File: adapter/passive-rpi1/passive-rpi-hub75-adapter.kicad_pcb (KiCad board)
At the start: 2 copper layers, 37 x 19 mm, 2 parts, among them P1 RPi-Header

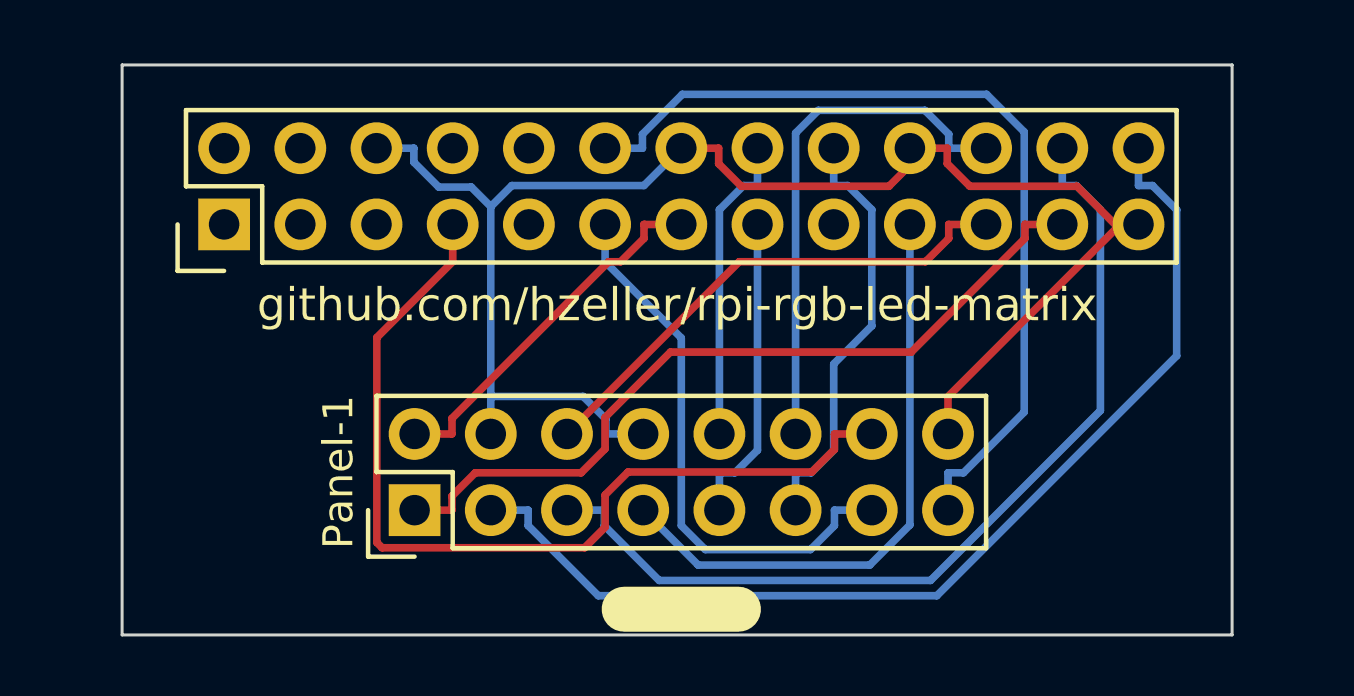
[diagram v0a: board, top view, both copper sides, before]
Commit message: o the connector is ambiguous, so make labelling a bit more obvious.
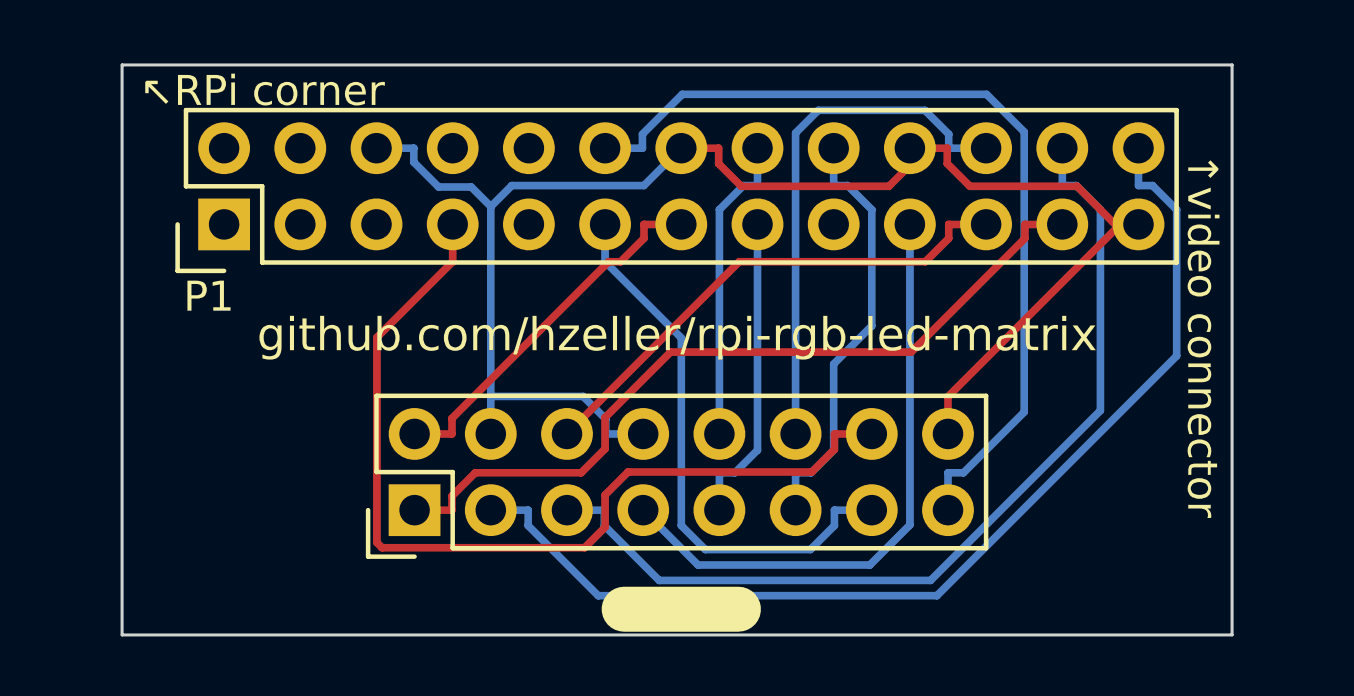
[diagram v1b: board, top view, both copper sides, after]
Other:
- board text added: "↑video connector"
- board text added: "↖RPi corner"
